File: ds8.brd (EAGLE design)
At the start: 85 x 50 mm, 79 parts, among them Q1 BC850, Q2 BC850, Q3 BC850, U1 LM13700M, U2 LM324, U3 LM324, U4 LM741D

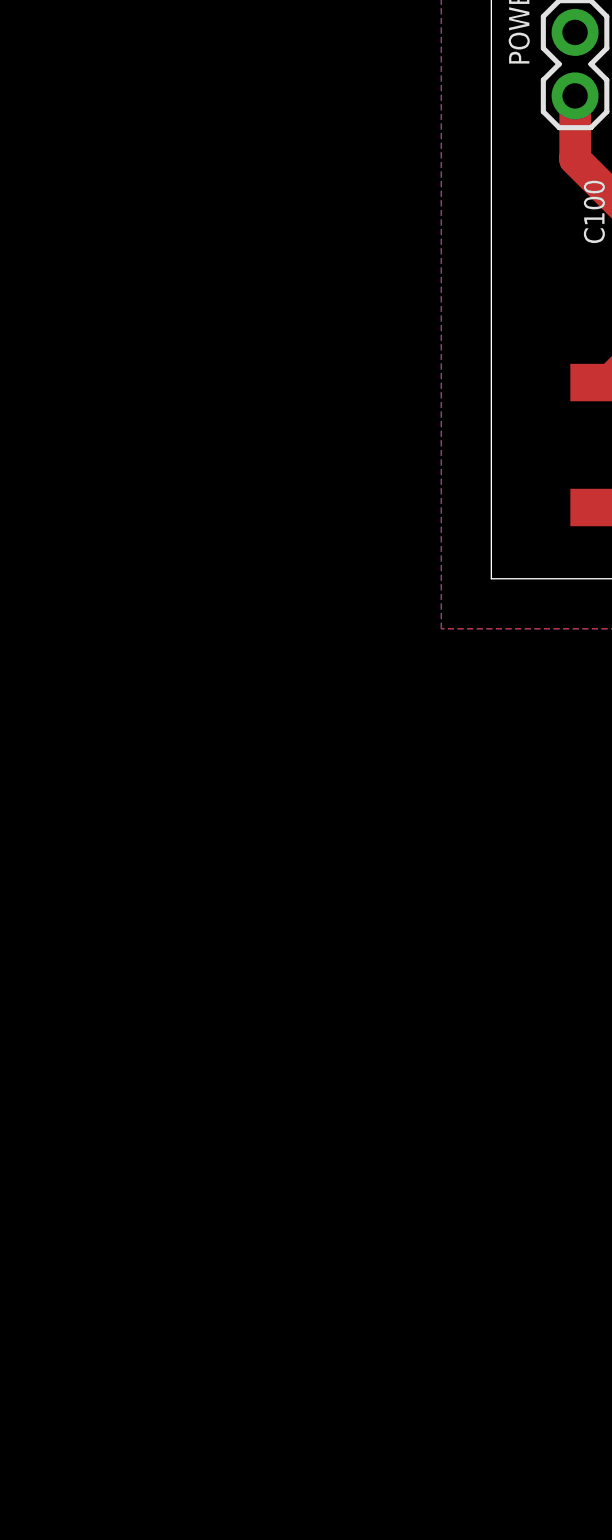
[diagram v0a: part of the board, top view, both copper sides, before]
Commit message: added regulator for mcu
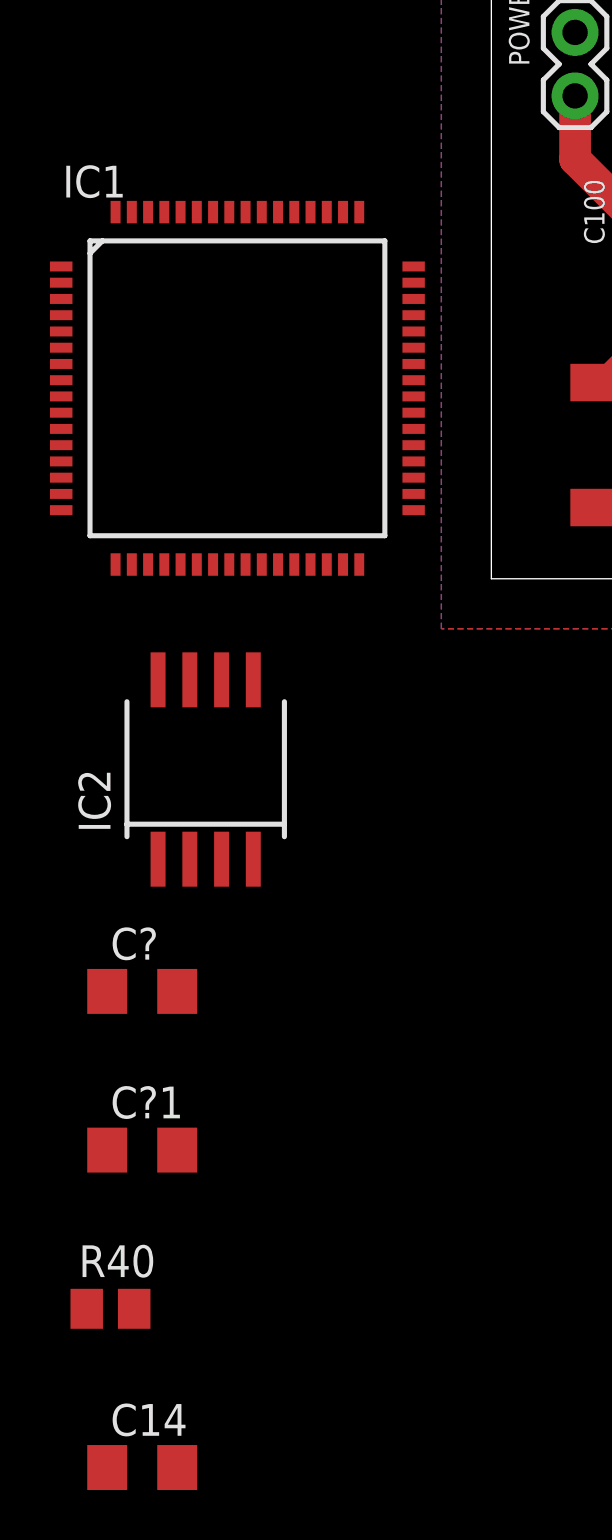
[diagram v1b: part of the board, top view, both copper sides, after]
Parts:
- added C14: 10n, rcl:C1206
- added C?, C?1: 100n, rcl:C1206
- added IC1: TM4C1230C3PM, TM4:LQFP_64
- added IC2: TPS77333, texas:SOP-08
- added R40: 10k, rcl:M0805
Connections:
- new net GNDA: IC1.3
- new net N$18: IC2.2, R40.1
- new net N$6: C14.2, IC1.25
- new net VDD: C?1.2, IC1.11, IC1.26, IC1.42, IC1.54, IC2.1, IC2.7, IC2.8, R40.2
- new net VDDA: IC1.2
- new net VDDC: IC1.56
- net GND: now also C14.1, C?.1, C?1.1, IC1.12, IC1.27, IC1.39, IC1.55, IC2.3, IC2.4
- net VCC: now also C?.2, IC2.5, IC2.6
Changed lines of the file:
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@@
 <?xml version="1.0" encoding="utf-8"?>
 <!DOCTYPE eagle SYSTEM "eagle.dtd">
-<eagle version="6.1">
+<eagle version="6.3">
 <drawing>
 <settings>
@@
 </class>
 </classes>
-<designrules>
+<designrules name="default">
 <description language="de">&lt;b&gt;EAGLE Design Rules&lt;/b&gt;
 &lt;p&gt;
@@
 <attribute name="VALUE" x="36.37" y="1.54" size="0.6096" layer="27"/>
 </element>
+<element name="IC1" library="TM4" package="LQFP_64" value="TM4C1230C3PM" x="-10.16" y="7.62"/>
+<element name="IC2" library="texas" package="SOP-08" value="TPS77333" x="-11.43" y="-7.62">
+<attribute name="OC_NEWARK" value="02M1919" x="-11.43" y="-7.62" size="1.778" layer="27" display="off"/>
+<attribute name="MPN" value="TPS77333DGK" x="-11.43" y="-7.62" size="1.778" layer="27" display="off"/>
+<attribute name="MF" value="TEXAS INSTRUMENTS" x="-11.43" y="-7.62" size="1.778" layer="27" display="off"/>
+<attribute name="OC_FARNELL" value="1510195" x="-11.43" y="-7.62" size="1.778" layer="27" display="off"/>
+</element>
+<element name="C?" library="rcl" package="C1206" value="100n" x="-13.97" y="-16.51"/>
+<element name="C?1" library="rcl" package="C1206" value="100n" x="-13.97" y="-22.86"/>
+<element name="R40" library="rcl" package="M0805" value="10k" x="-15.24" y="-29.21"/>
+<element name="C14" library="rcl" package="C1206" value="10n" x="-13.97" y="-35.56"/>
 </elements>
 <signals>
@@
 <via x="24.13" y="31.75" extent="1-16" drill="0.6"/>
 <via x="31.115" y="40.64" extent="1-16" drill="0.6"/>
+<contactref element="IC1" pad="12"/>
+<contactref element="IC1" pad="27"/>
+<contactref element="IC1" pad="39"/>
+<contactref element="IC1" pad="55"/>
+<contactref element="IC2" pad="4"/>
+<contactref element="IC2" pad="3"/>
+<contactref element="C?" pad="1"/>
+<contactref element="C?1" pad="1"/>
+<contactref element="C14" pad="1"/>
+<wire x1="56.69" y1="34.655" x2="69.39" y2="47.26" width="0" layer="19" extent="1-1"/>
+<wire x1="56.69" y1="32.02" x2="56.69" y2="34.655" width="0" layer="19" extent="1-1"/>
+<wire x1="63.675" y1="28.33" x2="56.69" y2="32.02" width="0" layer="19" extent="1-1"/>
+<wire x1="63.04" y1="25.67" x2="63.675" y2="28.33" width="0" layer="19" extent="1-1"/>
+<wire x1="48.2953" y1="26.94" x2="56.69" y2="32.02" width="0" layer="19" extent="1-1"/>
+<wire x1="41.45" y1="32.02" x2="48.2953" y2="26.94" width="0" layer="19" extent="1-1"/>
+<wire x1="41.45" y1="34.56" x2="41.45" y2="32.02" width="0" layer="19" extent="1-1"/>
+<wire x1="43.99" y1="34.655" x2="41.45" y2="34.56" width="0" layer="19" extent="1-1"/>
+<wire x1="38.91" y1="30.43" x2="41.45" y2="32.02" width="0" layer="19" extent="1-1"/>
+<wire x1="33.83" y1="30.43" x2="38.91" y2="30.43" width="0" layer="19" extent="1-1"/>
+<wire x1="33.83" y1="34.88" x2="33.83" y2="30.43" width="0" layer="19" extent="1-1"/>
+<wire x1="28.75" y1="30.43" x2="33.83" y2="30.43" width="0" layer="19" extent="1-1"/>
+<wire x1="24.13" y1="31.75" x2="28.75" y2="30.43" width="0" layer="19" extent="1-1"/>
+<wire x1="35.735" y1="25.035" x2="33.83" y2="30.43" width="0" layer="19" extent="1-1"/>
+<wire x1="33.83" y1="40.78" x2="33.83" y2="34.88" width="0" layer="19" extent="1-1"/>
+<wire x1="31.115" y1="40.64" x2="33.83" y2="40.78" width="0" layer="19" extent="1-1"/>
+<wire x1="21.9047" y1="25.035" x2="24.13" y2="31.75" width="0" layer="19" extent="1-1"/>
+<wire x1="38.91" y1="47.26" x2="33.83" y2="40.78" width="0" layer="19" extent="1-1"/>
+<wire x1="41.45" y1="47.26" x2="38.91" y2="47.26" width="0" layer="19" extent="1-1"/>
+<wire x1="49.07" y1="47.26" x2="41.45" y2="47.26" width="0" layer="19" extent="1-1"/>
+<wire x1="51.44" y1="17.73" x2="48.2953" y2="26.94" width="0" layer="19" extent="1-1"/>
+<wire x1="46.99" y1="13.97" x2="51.44" y2="17.73" width="0" layer="19" extent="1-1"/>
+<wire x1="43.99" y1="11.38" x2="46.99" y2="13.97" width="0" layer="19" extent="1-1"/>
+<wire x1="38.91" y1="11.83" x2="43.99" y2="11.38" width="0" layer="19" extent="1-1"/>
+<wire x1="33.83" y1="11.83" x2="38.91" y2="11.83" width="0" layer="19" extent="1-1"/>
+<wire x1="51.61" y1="11.065" x2="46.99" y2="13.97" width="0" layer="19" extent="1-1"/>
+<wire x1="56.055" y1="11.5984" x2="51.61" y2="11.065" width="0" layer="19" extent="1-1"/>
+<wire x1="29.845" y1="7.62" x2="33.83" y2="11.83" width="0" layer="19" extent="1-1"/>
+<wire x1="27.54" y1="16.145" x2="33.83" y2="11.83" width="0" layer="19" extent="1-1"/>
+<wire x1="16.05" y1="14.97" x2="27.54" y2="16.145" width="0" layer="19" extent="1-1"/>
+<wire x1="8.43" y1="17.91" x2="16.05" y2="14.97" width="0" layer="19" extent="1-1"/>
+<wire x1="3.35" y1="21.86" x2="8.43" y2="17.91" width="0" layer="19" extent="1-1"/>
+<wire x1="3.35" y1="26.94" x2="3.35" y2="21.86" width="0" layer="19" extent="1-1"/>
+<wire x1="8.43" y1="30.43" x2="3.35" y2="26.94" width="0" layer="19" extent="1-1"/>
+<wire x1="10.16" y1="33.02" x2="8.43" y2="30.43" width="0" layer="19" extent="1-1"/>
+<wire x1="8.43" y1="34.88" x2="10.16" y2="33.02" width="0" layer="19" extent="1-1"/>
+<wire x1="8.255" y1="39.37" x2="8.43" y2="34.88" width="0" layer="19" extent="1-1"/>
+<wire x1="8.43" y1="41.23" x2="8.255" y2="39.37" width="0" layer="19" extent="1-1"/>
+<wire x1="3.35" y1="37.1" x2="8.255" y2="39.37" width="0" layer="19" extent="1-1"/>
+<wire x1="15.86" y1="5.35" x2="16.05" y2="14.97" width="0" layer="19" extent="1-1"/>
+<wire x1="18.59" y1="47.26" x2="8.43" y2="41.23" width="0" layer="19" extent="1-1"/>
+<wire x1="67.95" y1="11.38" x2="56.055" y2="11.5984" width="0" layer="19" extent="1-1"/>
+<wire x1="78.11" y1="9.48" x2="67.95" y2="11.38" width="0" layer="19" extent="1-1"/>
+<wire x1="-9.185" y1="14.67" x2="3.35" y2="21.86" width="0" layer="19" extent="1-1"/>
+<wire x1="-3.11" y1="6.645" x2="-9.185" y2="14.67" width="0" layer="19" extent="1-1"/>
+<wire x1="-8.535" y1="0.57" x2="-3.11" y2="6.645" width="0" layer="19" extent="1-1"/>
+<wire x1="-17.21" y1="5.345" x2="-8.535" y2="0.57" width="0" layer="19" extent="1-1"/>
+<wire x1="-9.525" y1="-11.22" x2="-8.535" y2="0.57" width="0" layer="19" extent="1-1"/>
+<wire x1="-10.795" y1="-11.22" x2="-9.525" y2="-11.22" width="0" layer="19" extent="1-1"/>
+<wire x1="-15.37" y1="-16.51" x2="-10.795" y2="-11.22" width="0" layer="19" extent="1-1"/>
+<wire x1="-15.37" y1="-22.86" x2="-15.37" y2="-16.51" width="0" layer="19" extent="1-1"/>
+<wire x1="-15.37" y1="-35.56" x2="-15.37" y2="-22.86" width="0" layer="19" extent="1-1"/>
+<wire x1="82.09" y1="28.21" x2="63.675" y2="28.33" width="0" layer="19" extent="1-1"/>
 </signal>
 <signal name="VCC">
@@
 <wire x1="9.065" y1="22.05" x2="13.795" y2="17.32" width="0.6096" layer="1"/>
 <wire x1="13.795" y1="17.32" x2="16.05" y2="17.32" width="0.6096" layer="1"/>
+<contactref element="IC2" pad="5"/>
+<contactref element="IC2" pad="6"/>
+<contactref element="C?" pad="2"/>
+<wire x1="-10.795" y1="-4.045" x2="-12.57" y2="-16.51" width="0" layer="19" extent="1-1"/>
+<wire x1="-9.525" y1="-4.045" x2="-10.795" y2="-4.045" width="0" layer="19" extent="1-1"/>
+<wire x1="4.66" y1="2.85" x2="-9.525" y2="-4.045" width="0" layer="19" extent="1-1"/>
 </signal>
 <signal name="N$5">
@@
 <wire x1="43.99" y1="47.26" x2="43.99" y2="43.13" width="0.4064" layer="1"/>
 </signal>
+<signal name="VDDA">
+<contactref element="IC1" pad="2"/>
+</signal>
+<signal name="GNDA">
+<contactref element="IC1" pad="3"/>
+</signal>
+<signal name="VDD">
+<contactref element="IC1" pad="11"/>
+<contactref element="IC1" pad="42"/>
+<contactref element="IC1" pad="54"/>
+<contactref element="IC2" pad="7"/>
+<contactref element="IC2" pad="8"/>
+<contactref element="IC2" pad="1"/>
+<contactref element="C?1" pad="2"/>
+<contactref element="R40" pad="2"/>
+<contactref element="IC1" pad="26"/>
+<wire x1="-12.57" y1="-22.86" x2="-14.29" y2="-29.21" width="0" layer="19" extent="1-1"/>
+<wire x1="-13.335" y1="-11.22" x2="-12.57" y2="-22.86" width="0" layer="19" extent="1-1"/>
+<wire x1="-13.335" y1="-4.045" x2="-13.335" y2="-11.22" width="0" layer="19" extent="1-1"/>
+<wire x1="-12.065" y1="-4.045" x2="-13.335" y2="-4.045" width="0" layer="19" extent="1-1"/>
+<wire x1="-9.185" y1="0.57" x2="-12.065" y2="-4.045" width="0" layer="19" extent="1-1"/>
+<wire x1="-17.21" y1="5.995" x2="-9.185" y2="0.57" width="0" layer="19" extent="1-1"/>
+<wire x1="-3.11" y1="8.595" x2="-9.185" y2="0.57" width="0" layer="19" extent="1-1"/>
+<wire x1="-8.535" y1="14.67" x2="-3.11" y2="8.595" width="0" layer="19" extent="1-1"/>
+</signal>
+<signal name="VDDC">
+<contactref element="IC1" pad="56"/>
+</signal>
+<signal name="N$18">
+<contactref element="IC2" pad="2"/>
+<contactref element="R40" pad="1"/>
+<wire x1="-12.065" y1="-11.22" x2="-16.19" y2="-29.21" width="0" layer="19" extent="1-1"/>
+</signal>
+<signal name="N$6">
+<contactref element="IC1" pad="25"/>
+<contactref element="C14" pad="2"/>
+<wire x1="-9.835" y1="0.57" x2="-12.57" y2="-35.56" width="0" layer="19" extent="1-1"/>
+</signal>
 </signals>

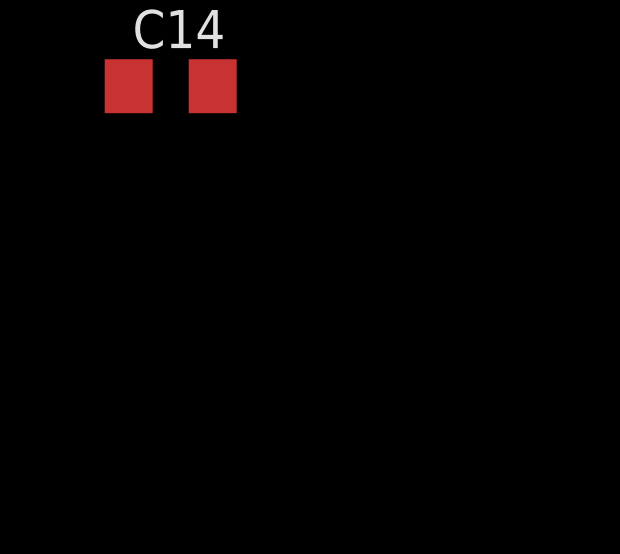
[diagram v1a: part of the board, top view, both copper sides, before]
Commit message: added dac
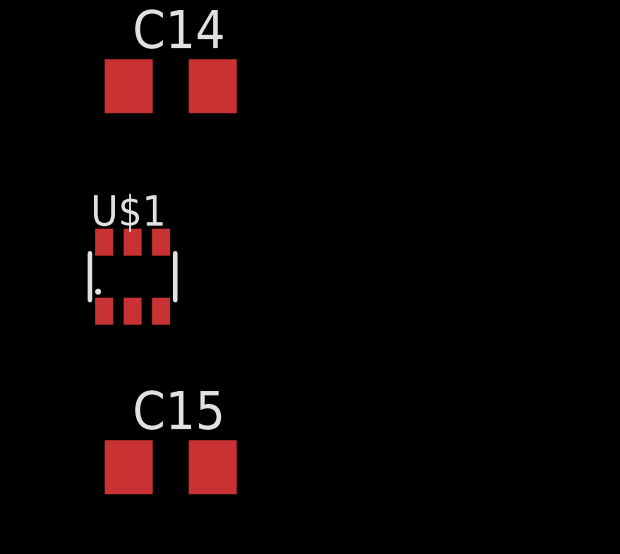
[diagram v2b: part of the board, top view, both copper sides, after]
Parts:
- added C15: 3uF, rcl:C1206
- added U$1: DAC7512, ds8:SOT-23-6
- C14: value 10n -> 3uF
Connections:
- new net /RESET: IC1.38, IC2.2, R40.2
- new net ARM_SSI0_CLK: IC1.19
- new net ARM_SSI0_FS: IC1.20, U$1.5, U$1.6
- new net ARM_SSI0_TX: IC1.22, U$1.4
- new net N$26: C15.2
- new net N$35: IC1.54
- net CVIN: now also U$1.1
- net GND: now also C15.1, U$1.2
- net N$18: now also IC1.42; no longer IC2.2, R40.1
- net VCC: now also U$1.3
- net VDD: now also R40.1; no longer IC1.42, IC1.54, R40.2
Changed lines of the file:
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@@
 <element name="C?1" library="rcl" package="C1206" value="100n" x="-13.97" y="-22.86"/>
 <element name="R40" library="rcl" package="M0805" value="10k" x="-15.24" y="-29.21"/>
-<element name="C14" library="rcl" package="C1206" value="10n" x="-13.97" y="-35.56"/>
+<element name="C14" library="rcl" package="C1206" value="3uF" x="-13.97" y="-35.56"/>
+<element name="U$1" library="ds8" package="SOT-23-6" value="DAC7512" x="-15.24" y="-41.91"/>
+<element name="C15" library="rcl" package="C1206" value="3uF" x="-13.97" y="-48.26"/>
 </elements>
 <signals>
@@
 <contactref element="C?1" pad="1"/>
 <contactref element="C14" pad="1"/>
+<contactref element="U$1" pad="2"/>
+<contactref element="C15" pad="1"/>
 <wire x1="56.69" y1="34.655" x2="69.39" y2="47.26" width="0" layer="19" extent="1-1"/>
 <wire x1="56.69" y1="32.02" x2="56.69" y2="34.655" width="0" layer="19" extent="1-1"/>
@@
 <wire x1="-15.37" y1="-22.86" x2="-15.37" y2="-16.51" width="0" layer="19" extent="1-1"/>
 <wire x1="-15.37" y1="-35.56" x2="-15.37" y2="-22.86" width="0" layer="19" extent="1-1"/>
+<wire x1="-15.24" y1="-43.06" x2="-15.37" y2="-35.56" width="0" layer="19" extent="1-1"/>
+<wire x1="-15.37" y1="-48.26" x2="-15.24" y2="-43.06" width="0" layer="19" extent="1-1"/>
 <wire x1="82.09" y1="28.21" x2="63.675" y2="28.33" width="0" layer="19" extent="1-1"/>
 </signal>
@@
 <contactref element="IC2" pad="6"/>
 <contactref element="C?" pad="2"/>
+<contactref element="U$1" pad="3"/>
+<wire x1="-12.57" y1="-16.51" x2="-14.29" y2="-43.06" width="0" layer="19" extent="1-1"/>
 <wire x1="-10.795" y1="-4.045" x2="-12.57" y2="-16.51" width="0" layer="19" extent="1-1"/>
 <wire x1="-9.525" y1="-4.045" x2="-10.795" y2="-4.045" width="0" layer="19" extent="1-1"/>
@@
 <wire x1="45.895" y1="44.085" x2="4.62" y2="44.085" width="0.4064" layer="16"/>
 <wire x1="4.62" y1="44.085" x2="3.35" y2="42.18" width="0.4064" layer="16"/>
+<contactref element="U$1" pad="1"/>
+<wire x1="3.35" y1="39.64" x2="-16.19" y2="-43.06" width="0" layer="19" extent="1-1"/>
 </signal>
 <signal name="LFO2">
@@
 <signal name="VDD">
 <contactref element="IC1" pad="11"/>
-<contactref element="IC1" pad="42"/>
-<contactref element="IC1" pad="54"/>
 <contactref element="IC2" pad="7"/>
 <contactref element="IC2" pad="8"/>
 <contactref element="IC2" pad="1"/>
 <contactref element="C?1" pad="2"/>
-<contactref element="R40" pad="2"/>
 <contactref element="IC1" pad="26"/>
-<wire x1="-12.57" y1="-22.86" x2="-14.29" y2="-29.21" width="0" layer="19" extent="1-1"/>
+<contactref element="R40" pad="1"/>
+<wire x1="-12.57" y1="-22.86" x2="-16.19" y2="-29.21" width="0" layer="19" extent="1-1"/>
 <wire x1="-13.335" y1="-11.22" x2="-12.57" y2="-22.86" width="0" layer="19" extent="1-1"/>
 <wire x1="-13.335" y1="-4.045" x2="-13.335" y2="-11.22" width="0" layer="19" extent="1-1"/>
@@
 <wire x1="-9.185" y1="0.57" x2="-12.065" y2="-4.045" width="0" layer="19" extent="1-1"/>
 <wire x1="-17.21" y1="5.995" x2="-9.185" y2="0.57" width="0" layer="19" extent="1-1"/>
-<wire x1="-3.11" y1="8.595" x2="-9.185" y2="0.57" width="0" layer="19" extent="1-1"/>
-<wire x1="-8.535" y1="14.67" x2="-3.11" y2="8.595" width="0" layer="19" extent="1-1"/>
 </signal>
 <signal name="VDDC">
 <contactref element="IC1" pad="56"/>
-</signal>
-<signal name="N$18">
-<contactref element="IC2" pad="2"/>
-<contactref element="R40" pad="1"/>
-<wire x1="-12.065" y1="-11.22" x2="-16.19" y2="-29.21" width="0" layer="19" extent="1-1"/>
 </signal>
 <signal name="N$6">
@@
 <wire x1="-9.835" y1="0.57" x2="-12.57" y2="-35.56" width="0" layer="19" extent="1-1"/>
 </signal>
+<signal name="ARM_SSI0_FS">
+<contactref element="IC1" pad="20"/>
+<contactref element="U$1" pad="6"/>
+<contactref element="U$1" pad="5"/>
+<wire x1="-15.24" y1="-40.76" x2="-16.19" y2="-40.76" width="0" layer="19" extent="1-1"/>
+<wire x1="-13.085" y1="0.57" x2="-15.24" y2="-40.76" width="0" layer="19" extent="1-1"/>
+</signal>
+<signal name="ARM_SSI0_CLK">
+<contactref element="IC1" pad="19"/>
+</signal>
+<signal name="ARM_SSI0_TX">
+<contactref element="IC1" pad="22"/>
+<contactref element="U$1" pad="4"/>
+<wire x1="-11.785" y1="0.57" x2="-14.29" y2="-40.76" width="0" layer="19" extent="1-1"/>
+</signal>
+<signal name="/RESET">
+<contactref element="IC2" pad="2"/>
+<contactref element="R40" pad="2"/>
+<contactref element="IC1" pad="38"/>
+<wire x1="-12.065" y1="-11.22" x2="-14.29" y2="-29.21" width="0" layer="19" extent="1-1"/>
+<wire x1="-3.11" y1="5.995" x2="-12.065" y2="-11.22" width="0" layer="19" extent="1-1"/>
+</signal>
+<signal name="N$18">
+<contactref element="IC1" pad="42"/>
+</signal>
+<signal name="N$26">
+<contactref element="C15" pad="2"/>
+</signal>
+<signal name="N$35">
+<contactref element="IC1" pad="54"/>
+</signal>
 </signals>

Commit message: clean up
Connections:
- removed net GNDA: IC1.3
- removed net N$18: IC1.42
- removed net N$35: IC1.54
- removed net VDDA: IC1.2
- net GND: now also IC1.3
- net N$5: no longer R5.2
- net VCC: now also R5.2; no longer R5.1
- net VDD: now also IC1.2, IC1.42, IC1.54
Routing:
- net VCC: track 181.4 -> 166.9 mm
- net N$5: track 24.5 -> 18.9 mm

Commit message: wire conflicts
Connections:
- removed net VDDC: IC1.56
- net N$36: now also IC1.56
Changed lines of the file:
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@@
 <contactref element="IC1" pad="55"/>
 <contactref element="IC1" pad="39"/>
+<contactref element="IC1" pad="27"/>
 <wire x1="56.69" y1="34.655" x2="69.39" y2="47.26" width="0" layer="19" extent="1-1"/>
 <wire x1="56.69" y1="32.02" x2="56.69" y2="34.655" width="0" layer="19" extent="1-1"/>
@@
 <wire x1="-3.11" y1="8.595" x2="-8.535" y2="14.67" width="0" layer="19" extent="1-1"/>
 </signal>
-<signal name="VDDC">
-<contactref element="IC1" pad="56"/>
-</signal>
 <signal name="N$6">
 <contactref element="IC1" pad="25"/>
@@
 <signal name="N$36">
 <contactref element="C15" pad="2"/>
+<contactref element="IC1" pad="56"/>
+<wire x1="-9.835" y1="14.67" x2="-12.57" y2="-48.26" width="0" layer="19" extent="1-1"/>
 </signal>
 </signals>
